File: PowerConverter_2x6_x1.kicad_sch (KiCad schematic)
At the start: 12 parts, among them J1 Conn_01x05, J2 Conn_01x05, J3 Conn_01x05, J4 Conn_01x05, J5 Regulator connector, J6 JST_SH_SM06B-SRSS-TB_1x06-1MP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, J7 Conn_01x04, U1 M24C02-FMN

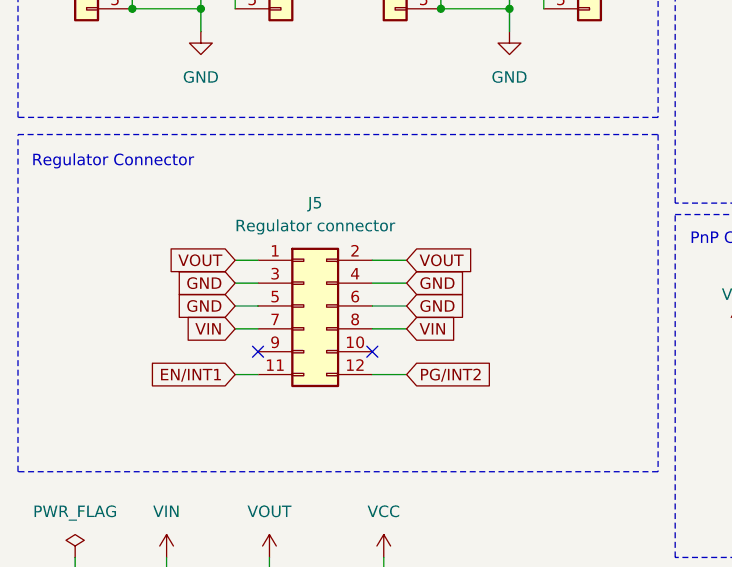
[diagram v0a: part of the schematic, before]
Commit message: Rotate regulator 90deg to have better connection to VIN and VOUT lines
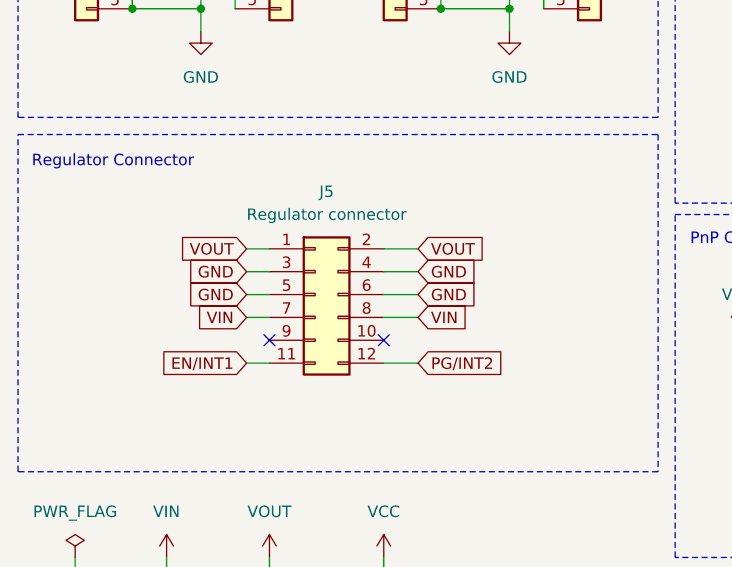
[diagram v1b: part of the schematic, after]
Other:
- moved on the sheet: J5
